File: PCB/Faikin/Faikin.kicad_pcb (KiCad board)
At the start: 2 copper layers, 70 x 70 mm, 44 parts, among them J1 1x5, J2 TC2030-USB-NL, J3 Reset, Q1 BSS138PS, U1 TPS562246, U4 ESP32-S3-MINI-1

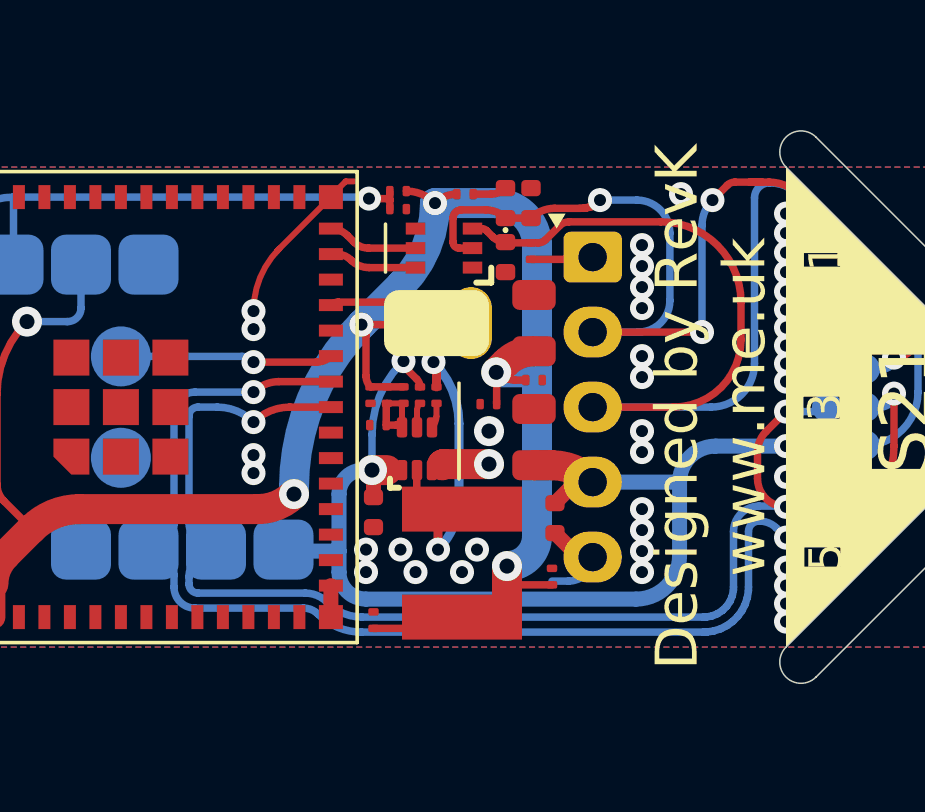
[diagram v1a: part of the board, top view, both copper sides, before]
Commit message: Tweak layout, and more test points
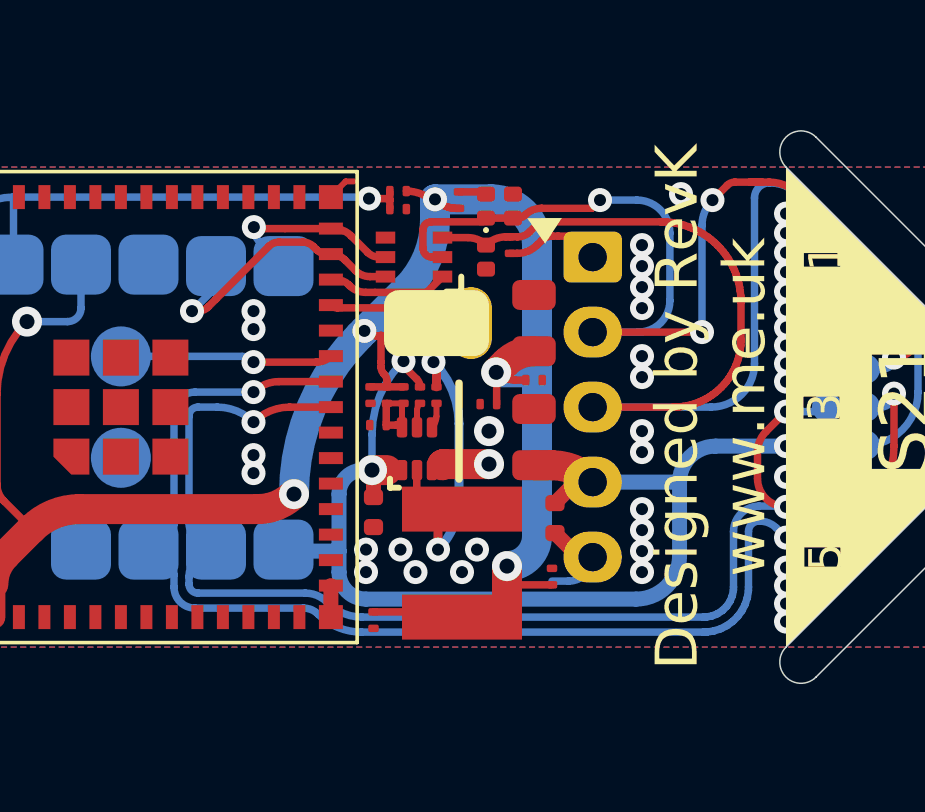
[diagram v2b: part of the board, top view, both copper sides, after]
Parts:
- added TP10: TestPoint, RevK:PAD-2mm, B.Cu at (135.2, 60.3)
- added TP9: TestPoint, RevK:PAD-2mm, B.Cu at (133.0, 60.3)
- moved Q1 1.04 mm to (139.6, 60.0)
- moved R1 0.73 mm to (142.8, 59.6)
- moved D4 0.66 mm to (142.0, 58.3)
- moved D2 0.65 mm to (142.0, 60.0)
- moved D3 0.61 mm to (142.9, 58.3)
- moved R2 0.28 mm to (141.1, 58.1), turned to 90 degrees
- turned C2 to 90 degrees
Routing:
- net RX: track 2.75 -> 9.55 mm, vias 0 -> 1
- net TX: track 3.02 -> 6.40 mm, vias 0 -> 1
- net Net-(J1-Pin_3): track 42.5 -> 43.6 mm
- net GND: track 11.4 -> 10.6 mm
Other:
- board text added: "RX"
- board text added: "TX"

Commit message: Fiducials
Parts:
- added FID1: Fiducial, Fiducial:Fiducial_1mm_Mask2mm, F.Cu at (114.8, 65.0)
- added FID2: Fiducial, Fiducial:Fiducial_1mm_Mask2mm, F.Cu at (129.8, 55.0)
- added FID3: Fiducial, Fiducial:Fiducial_1mm_Mask2mm, F.Cu at (129.8, 75.0)
- moved U4 0.08 mm to (129.8, 65.0)
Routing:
- net RST: track 18.8 -> 19.8 mm
- net RX: track 9.55 -> 8.62 mm

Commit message: Tidy
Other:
- board text removed: "Baking for D1 is not required"

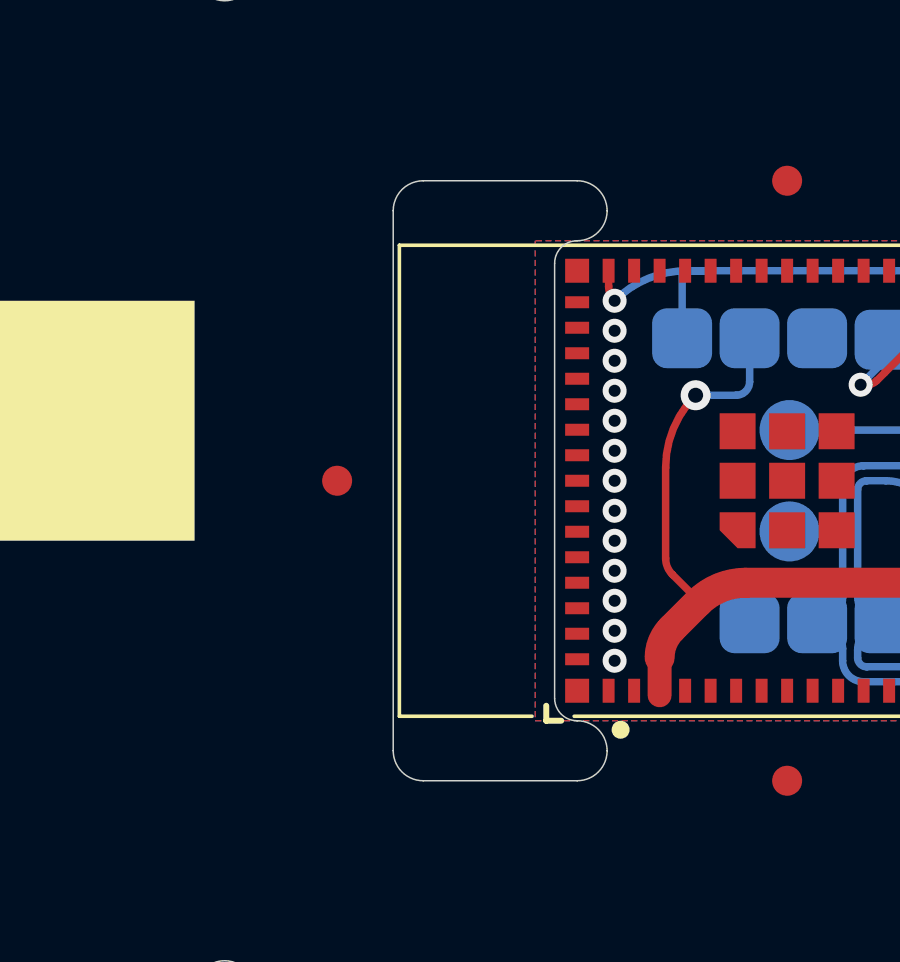
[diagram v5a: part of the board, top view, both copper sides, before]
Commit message: Thicker top
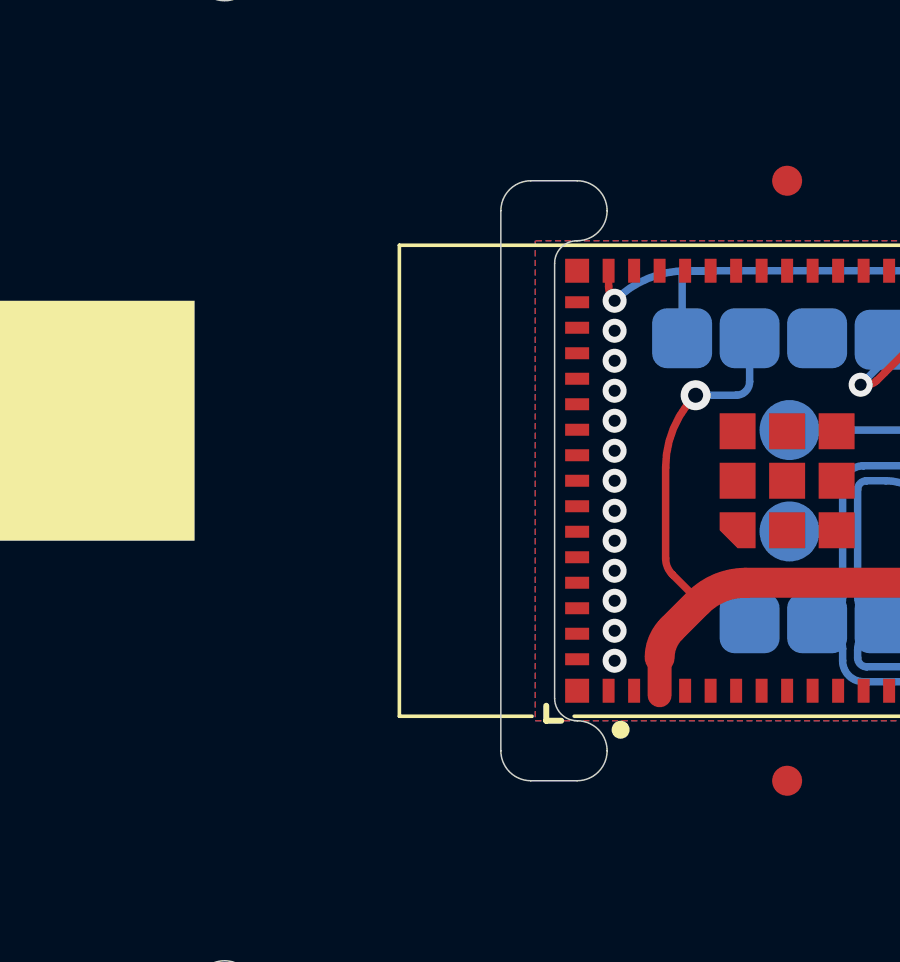
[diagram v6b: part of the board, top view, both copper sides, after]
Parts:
- removed FID1: Fiducial, Fiducial:Fiducial_1mm_Mask2mm

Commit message: Tweak
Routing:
- net +3.3V: track 66.7 -> 66.0 mm
